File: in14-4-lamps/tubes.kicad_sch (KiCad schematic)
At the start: 13 parts

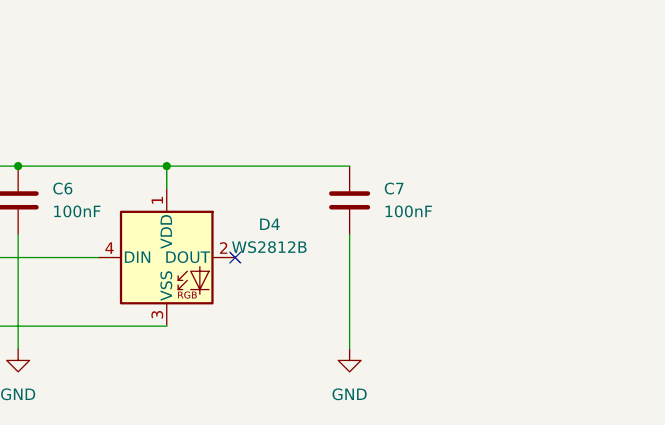
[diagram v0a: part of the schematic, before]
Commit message: add button and ws2812 connector
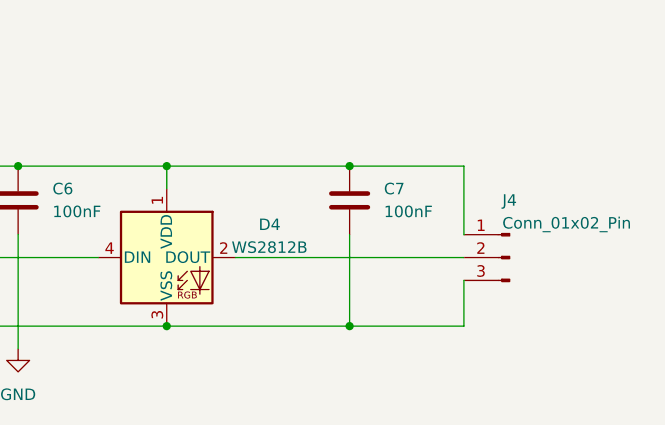
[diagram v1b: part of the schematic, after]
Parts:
- added J4: Conn_01x02_Pin, Connector_PinHeader_2.54mm:PinHeader_1x03_P2.54mm_Vertical, symbol Connector:Conn_01x03_Pin
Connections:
- net +5V: now also J4.1 (Pin_1)
- net GND: now also J4.3 (Pin_3)
- net at D4.2 (DOUT): now also J4.2 (Pin_2)
- no-connect marks 9 -> 8
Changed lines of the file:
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@@
   (junction (at 50.8 129.54) (diameter 0) (color 0 0 0 0)
   )
+  (junction (at 185.42 147.32) (diameter 0) (color 0 0 0 0)
+  )
   (junction (at 69.85 129.54) (diameter 0) (color 0 0 0 0)
   )
+  (junction (at 165.1 147.32) (diameter 0) (color 0 0 0 0)
+  )
   (junction (at 127 147.32) (diameter 0) (color 0 0 0 0)
   )
@@
   )
   (junction (at 109.22 129.54) (diameter 0) (color 0 0 0 0)
+  )
+  (junction (at 185.42 129.54) (diameter 0) (color 0 0 0 0)
   )
   (junction (at 165.1 129.54) (diameter 0) (color 0 0 0 0)
@@
   (no_connect (at 147.32 57.15))
   (no_connect (at 96.52 34.29))
-  (no_connect (at 172.72 139.7))
   (no_connect (at 96.52 57.15))
   (no_connect (at 198.12 57.15))
@@
     (stroke (width 0) (type default))
   )
+  (wire (pts (xy 185.42 137.16) (xy 185.42 147.32))
+    (stroke (width 0) (type default))
+  )
   (wire (pts (xy 38.1 81.28) (xy 38.1 83.82))
     (stroke (width 0) (type default))
@@
     (stroke (width 0) (type default))
   )
+  (wire (pts (xy 198.12 142.24) (xy 198.12 147.32))
+    (stroke (width 0) (type default))
+  )
   (wire (pts (xy 180.34 34.29) (xy 182.88 34.29))
     (stroke (width 0) (type default))
@@
     (stroke (width 0) (type default))
   )
+  (wire (pts (xy 172.72 139.7) (xy 198.12 139.7))
+    (stroke (width 0) (type default))
+  )
   (wire (pts (xy 27.94 41.91) (xy 30.48 41.91))
     (stroke (width 0) (type default))
@@
     (stroke (width 0) (type default))
   )
-  (wire (pts (xy 185.42 137.16) (xy 185.42 149.86))
-    (stroke (width 0) (type default))
-  )
   (wire (pts (xy 129.54 46.99) (xy 132.08 46.99))
     (stroke (width 0) (type default))
@@
     (stroke (width 0) (type default))
   )
+  (wire (pts (xy 198.12 137.16) (xy 198.12 129.54))
+    (stroke (width 0) (type default))
+  )
+  (wire (pts (xy 185.42 147.32) (xy 165.1 147.32))
+    (stroke (width 0) (type default))
+  )
   (wire (pts (xy 129.54 44.45) (xy 132.08 44.45))
     (stroke (width 0) (type default))
@@
     (stroke (width 0) (type default))
   )
+  (wire (pts (xy 198.12 147.32) (xy 185.42 147.32))
+    (stroke (width 0) (type default))
+  )
   (wire (pts (xy 129.54 39.37) (xy 132.08 39.37))
     (stroke (width 0) (type default))
@@
   )
   (wire (pts (xy 88.9 129.54) (xy 109.22 129.54))
+    (stroke (width 0) (type default))
+  )
+  (wire (pts (xy 198.12 129.54) (xy 185.42 129.54))
     (stroke (width 0) (type default))
   )
@@
     )
   )
-  (symbol (lib_id "power:GND") (at 185.42 149.86 0) (unit 1)
-    (in_bom yes) (on_board yes) (dnp no) (fields_autoplaced)
-    (property "Reference" "#PWR029" (at 185.42 156.21 0)
-      (effects (font (size 1.27 1.27)) hide)
-    )
-    (property "Value" "GND" (at 185.42 154.94 0)
-      (effects (font (size 1.27 1.27)))
-    )
-    (property "Footprint" "" (at 185.42 149.86 0)
-      (effects (font (size 1.27 1.27)) hide)
-    )
-    (property "Datasheet" "" (at 185.42 149.86 0)
+  (symbol (lib_id "Connector:Conn_01x03_Pin") (at 203.2 139.7 0) (mirror y) (unit 1)
+    (in_bom yes) (on_board yes) (dnp no)
+    (property "Reference" "J4" (at 203.2 133.35 0)
+      (effects (font (size 1.27 1.27)))
+    )
+    (property "Value" "Conn_01x02_Pin" (at 209.55 135.89 0)
+      (effects (font (size 1.27 1.27)))
+    )
+    (property "Footprint" "Connector_PinHeader_2.54mm:PinHeader_1x03_P2.54mm_Vertical" (at 203.2 139.7 0)
+      (effects (font (size 1.27 1.27)) hide)
+    )
+    (property "Datasheet" "~" (at 203.2 139.7 0)
       (effects (font (size 1.27 1.27)) hide)
     )
     (pin "1")
+    (pin "2")
+    (pin "3")
     (instances
       (project "nixie-clock-esp-32"
         (path "/cd8918ee-e986-4b1b-bef5-f32ed2eef1b1/06f34b52-5a6a-4de1-84d0-e5bfe04d78e4"
-          (reference "#PWR029") (unit 1)
+          (reference "J4") (unit 1)
         )
       )
